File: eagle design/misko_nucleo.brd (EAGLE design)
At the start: 115 x 115 mm, 131 parts, among them CN1 LiPo Battery, IC1 MC1525TT, IC101 ADXL345, IC102 74HCT1G32GW, IC2 TPS63031, IC3 FT230XS, IC4 RN4678_BT_MODULE, IC5 DS1394U-33+, IC6 MAX6818, IC7 SP3012-04UTG, Q1 ABM3B-8MHZ-10-1-U-T, Q2 BSS84, Q3 LFXTAL016178R, SW1 MICROJOYSTICK, SW2 PB6156RSL, SW3 PB6156RSL, U1 SN74LVC1G3157DBVR - BT switch, U2 ATMEGA1281-16AU, U3 TMP36GRTZ, U4 MCP73871-2AAI/ML, U5 SN74LVC1G3157DBVR - GPS switch, X1 FH12-30S-0.5SH

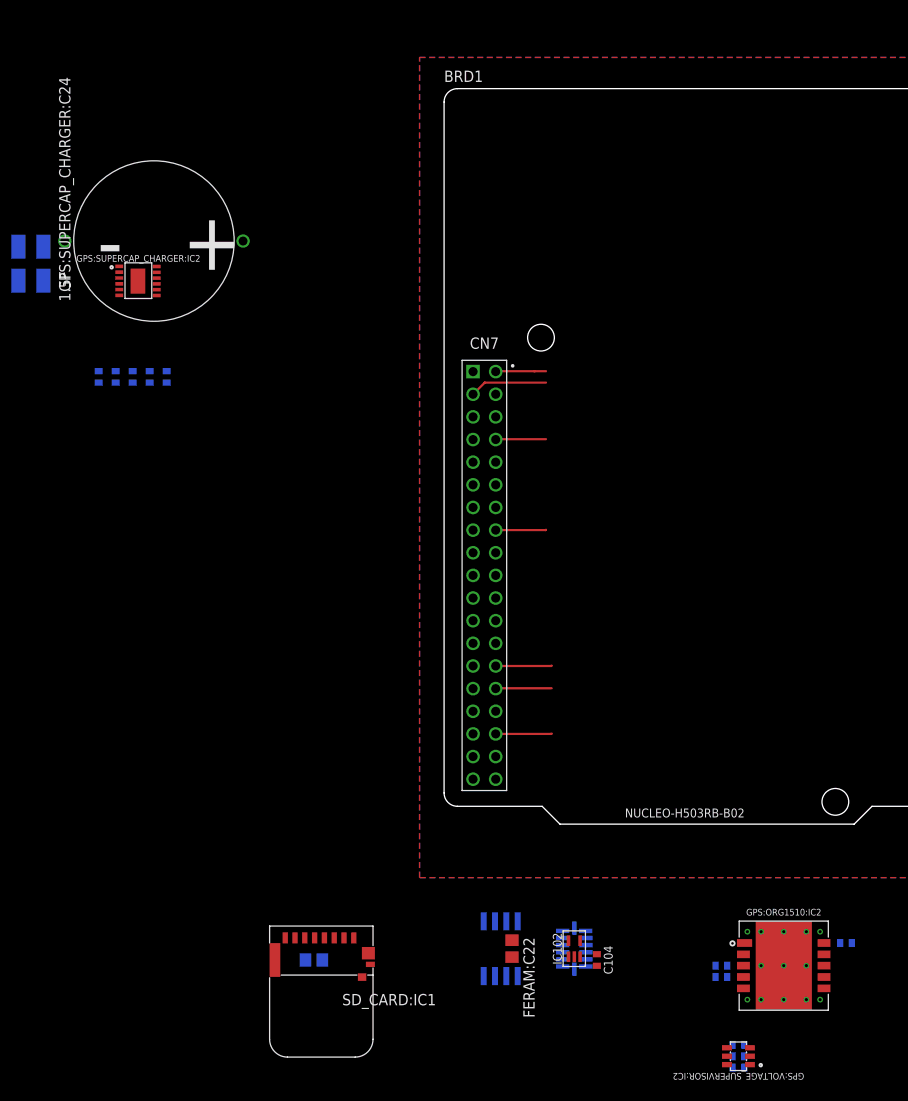
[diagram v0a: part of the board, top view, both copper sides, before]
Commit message: - corrected net names in modules
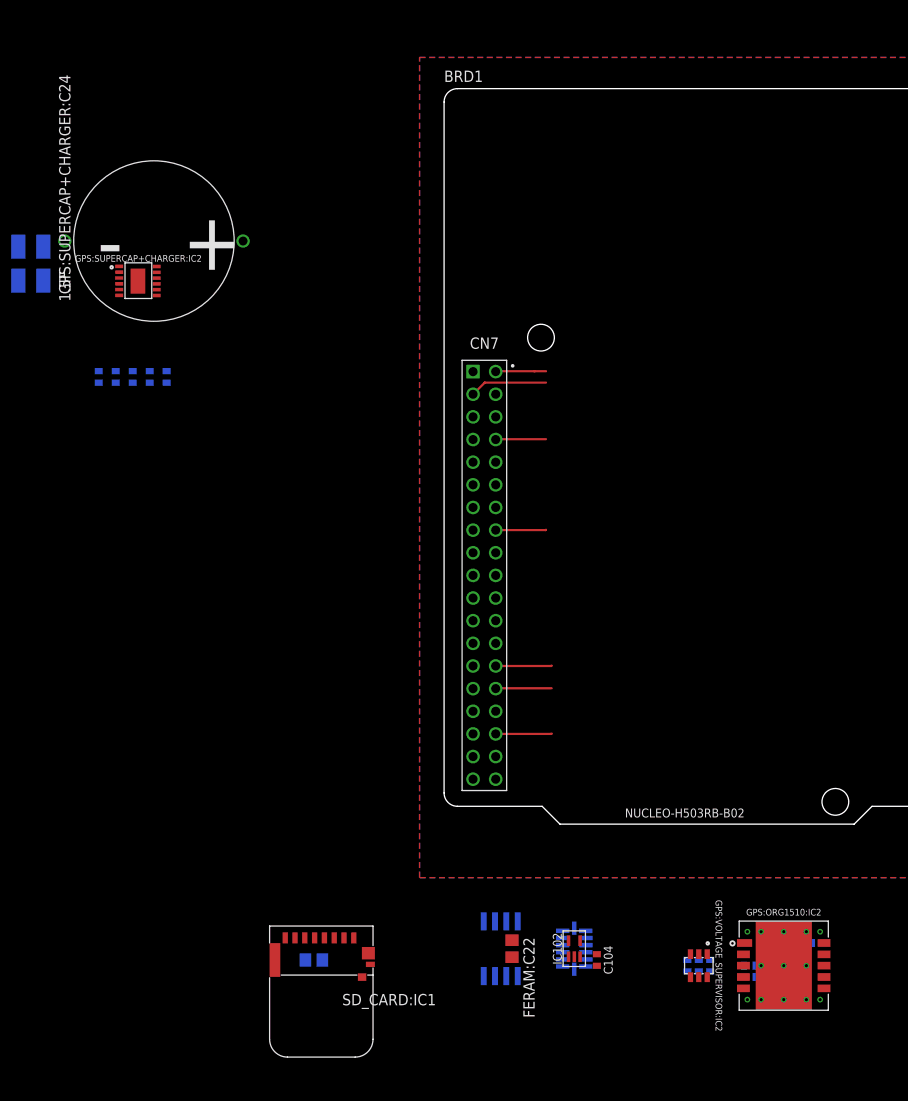
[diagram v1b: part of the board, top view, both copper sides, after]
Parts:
- moved GPS:VOLTAGE_SUPERVISOR:R18 11.9 mm to (29.8, -15.9), turned to 270 degrees
- moved GPS:VOLTAGE_SUPERVISOR:C2 11.1 mm to (28.6, -15.9), turned to 90 degrees
- moved GPS:VOLTAGE_SUPERVISOR:IC2 11.1 mm to (28.6, -15.9), turned to 270 degrees
- moved GPS:VOLTAGE_SUPERVISOR:C1 10.6 mm to (27.3, -15.9), turned to 90 degrees
- moved GPS:ORG1510:C31 3.18 mm to (41.9, -13.3), turned to 0 degrees
- moved GPS:ORG1510:C2 3.18 mm to (34.3, -17.1), turned to 180 degrees
- moved GPS:ORG1510:C22 3.18 mm to (34.3, -15.9), turned to 180 degrees
- renumbered GPS:SUPERCAP_CHARGER:C1 to GPS:SUPERCAP+CHARGER:C1, GPS:SUPERCAP_CHARGER:C24 to GPS:SUPERCAP+CHARGER:C24, GPS:SUPERCAP_CHARGER:C34 to GPS:SUPERCAP+CHARGER:C34, GPS:SUPERCAP_CHARGER:C38 to GPS:SUPERCAP+CHARGER:C38, GPS:SUPERCAP_CHARGER:IC2 to GPS:SUPERCAP+CHARGER:IC2, GPS:SUPERCAP_CHARGER:R14 to GPS:SUPERCAP+CHARGER:R14, GPS:SUPERCAP_CHARGER:R18 to GPS:SUPERCAP+CHARGER:R18, GPS:SUPERCAP_CHARGER:R40 to GPS:SUPERCAP+CHARGER:R40, GPS:SUPERCAP_CHARGER:R41 to GPS:SUPERCAP+CHARGER:R41
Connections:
- net GPS:SUPERCAP_CHARGER:EN renamed GPS:SUPERCAP+CHARGER:EN
- net GPS:SUPERCAP_CHARGER:PFI renamed GPS:SUPERCAP+CHARGER:PFI
- net GPS:SUPERCAP_CHARGER:PFI_RET renamed GPS:SUPERCAP+CHARGER:PFI_RET
- net GPS:SUPERCAP_CHARGER:PROG renamed GPS:SUPERCAP+CHARGER:PROG
- net GPS:SUPERCAP_CHARGER:VMID renamed GPS:SUPERCAP+CHARGER:VMID
- removed net GPS:VOLTAGE_SUPERVISOR:3V3: GPS:VOLTAGE_SUPERVISOR:C2.1, GPS:VOLTAGE_SUPERVISOR:IC2.VDD, GPS:VOLTAGE_SUPERVISOR:R18.2
- new net GPS:VOLTAGE_SUPERVISOR:SENSE: GPS:VOLTAGE_SUPERVISOR:C1.1, GPS:VOLTAGE_SUPERVISOR:IC2.SENSE
- net 3V3: now also GPS:VOLTAGE_SUPERVISOR:C2.1, GPS:VOLTAGE_SUPERVISOR:IC2.VDD, GPS:VOLTAGE_SUPERVISOR:R18.2
- net GPS:VGPS: no longer GPS:VOLTAGE_SUPERVISOR:C1.1, GPS:VOLTAGE_SUPERVISOR:IC2.SENSE

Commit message: - removed not needed components (crystal, voltage reference, etc.) from original schematic
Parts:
- removed C1, C16, C26: 0.1µF, resistor:C0805
- removed C19, C20, C23, C25: 1000µF, rcl:E5-10,5
- removed C2: 10µF, resistor:C0805
- removed C5, C9: 7pF, resistor:C0805
- removed CONN2: JTAG, JTAG 1.27mm 10pin header:TH-JTAG
- removed D1: 1N4148, Diode2:D0805
- removed IC1: MC1525TT, microchip:SOT23
- removed JP1: I2C, jumper:JP4
- removed L2: DL0805-33 33µH, rcl:L0805
- removed Q1: ABM3B-8MHZ-10-1-U-T, ABM3B-8MHZ-10-1-U-T - Quartz Resonator:SMT
- removed R1: 47k, rcl:R0805
- removed R3: 4k7, rcl:R0805
- removed R7, R8: 150k, rcl:R0805
- removed S1: RESET, Wurth_Elektronik_Electromechanic_Switch_rev17c:430152050836
- removed TP1, TP2, TP3: GND, testpad:P1-17Y
- removed TP11: Bluetooth Wakeup Pin, testpad:TP14R
- removed TP4: VCC, testpad:TP14R
- removed TP5: VLiIon Regulated, testpad:TP14R
- removed TP6: VGPS, testpad:TP14R
- removed TP7: Analogue Switch CRTL Pin, testpad:TP14R
- removed TP8: GPS Power CTRL Pin, testpad:B1,27
- removed U3: TMP36GRTZ, TMP36GRTZ:SOT95P280X145-5N
- moved D4 65.5 mm to (157.4, 113.3)
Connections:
- removed net N$31: C1.2, D1.A, R1.1
- net ADXL345_INT1_INTERRUPT_PIN: no longer JP1.3
- net ANALOG_SW_CTRL_PIN: no longer TP7.TP
- net AREF: no longer C2.1, IC1.2
- net AVCC: no longer C26.2, IC1.1, L2.2
- net BLUETOOTH_PROF_IND_PIN: no longer TP11.TP
- net GND: no longer C1.1, C16.2, C19.-, C2.2, C20.-, C23.-, C25.-, C26.1, C5.1, C9.1, CONN2.10_GND, CONN2.2_GND, IC1.3, JP1.1, Q1.GND1, Q1.GND2, R8.2, S1.1, S1.3, TP1.TP, U3.5
- net GPS_POWER_CTL_PIN: no longer TP8.TP
- net JTAG_TCL_PIN: no longer CONN2.1_JTAG_TCK
- net JTAG_TDI_PIN: no longer CONN2.9_JTAG_TDI
- net JTAG_TDO_PIN: no longer CONN2.3_JTAG_TDO
- net JTAG_TMS_PIN: no longer CONN2.5_JTAG_TMS
- net N$6: no longer C19.+, C20.+, C23.+, C25.+
- net RESET: no longer CONN2.6_JTAG_RST, R1.2, R3.2, S1.2, S1.4
- net RTC_INT_INTERRUPT_PIN: no longer JP1.4
- net TMP36_VSENSE_PIN: no longer U3.1
- net VCC: no longer C16.1, CONN2.4_VCC, D1.C, JP1.2, L2.1, R3.1, R7.1, TP3.TP, TP4.TP, U3.2, U3.4
- net VCC_SENSE_PIN: no longer R7.2, R8.1
- net VGPS: no longer TP6.TP
- net VUSB: no longer TP2.TP
- net V_LIION_REGULATED: no longer TP5.TP
- net XTAL1: no longer C9.2, Q1.Q2
- net XTAL2: no longer C5.2, Q1.Q1
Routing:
- net VCC: track 385.2 -> 275.0 mm, vias 15 -> 14
- net N$6: track 106.0 -> 0.00 mm
- net RESET: track 64.8 -> 0.00 mm, vias 3 -> 0
- net VGPS: track 52.4 -> 9.08 mm, vias 1 -> 0
- net GND: track 47.2 -> 25.2 mm, vias 37 -> 3
- net VCC_SENSE_PIN: track 14.1 -> 0.00 mm, vias 1 -> 0
- net TMP36_VSENSE_PIN: track 14.1 -> 0.00 mm, vias 3 -> 0
- net AVCC: track 12.1 -> 0.00 mm, vias 1 -> 0
- net JTAG_TDO_PIN: track 11.8 -> 0.00 mm, vias 2 -> 0
- net OLD_5V0: track 57.7 -> 46.4 mm, vias 6 -> 5
- net AREF: track 11.0 -> 0.00 mm, vias 1 -> 0
- net JTAG_TCL_PIN: track 10.1 -> 0.00 mm
- net V_LIION_REGULATED: track 41.0 -> 30.9 mm
- net JTAG_TDI_PIN: track 9.86 -> 0.00 mm
- net JTAG_TMS_PIN: track 9.47 -> 0.00 mm
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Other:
- board size 115 x 115 mm -> 115 x 73 mm
- board text removed: "BT PROF IND"
- board text removed: "GPS PWR CTRL"
- board text removed: "I2C"
- board text removed: "JTAG"
- board text removed: "RESET"

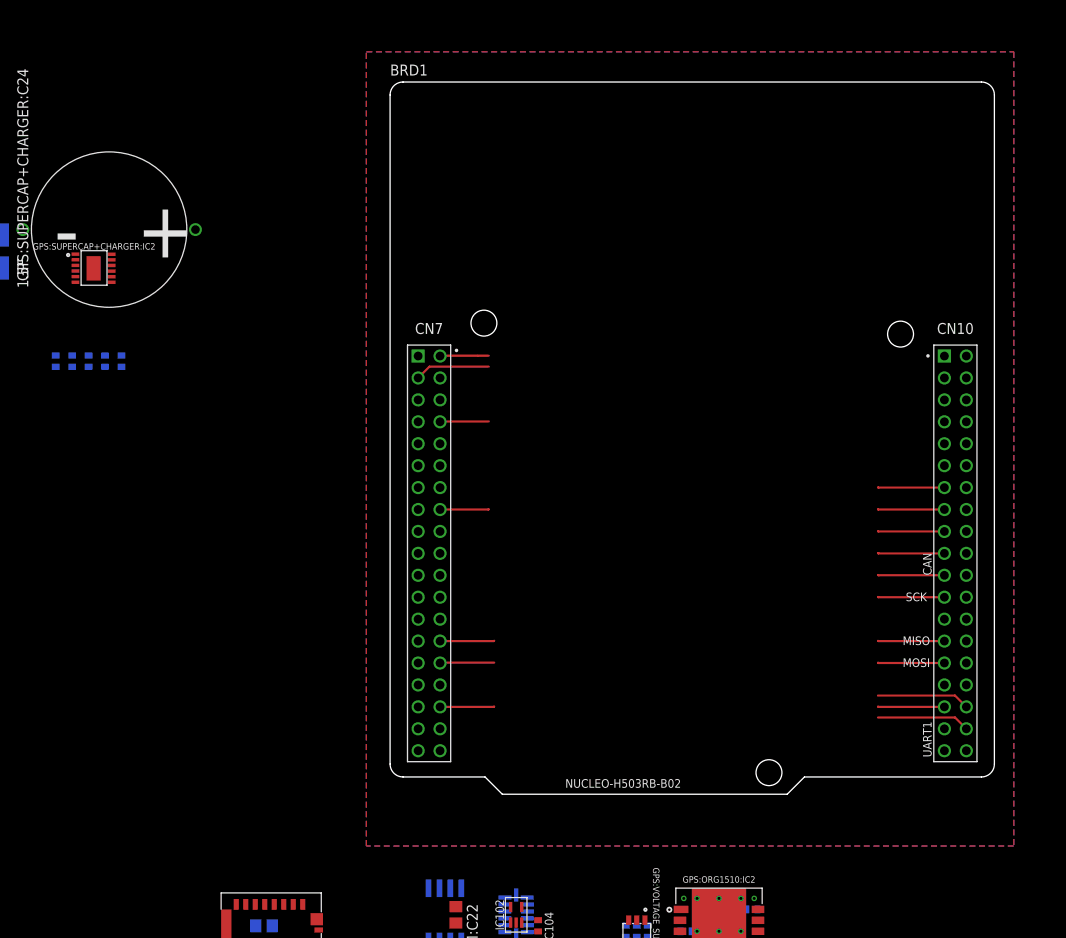
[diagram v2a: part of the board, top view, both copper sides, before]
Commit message: - added/coded and routed ORG1510-MK4 GPS module reset and LTC4425 SuperCap Charger enable pins
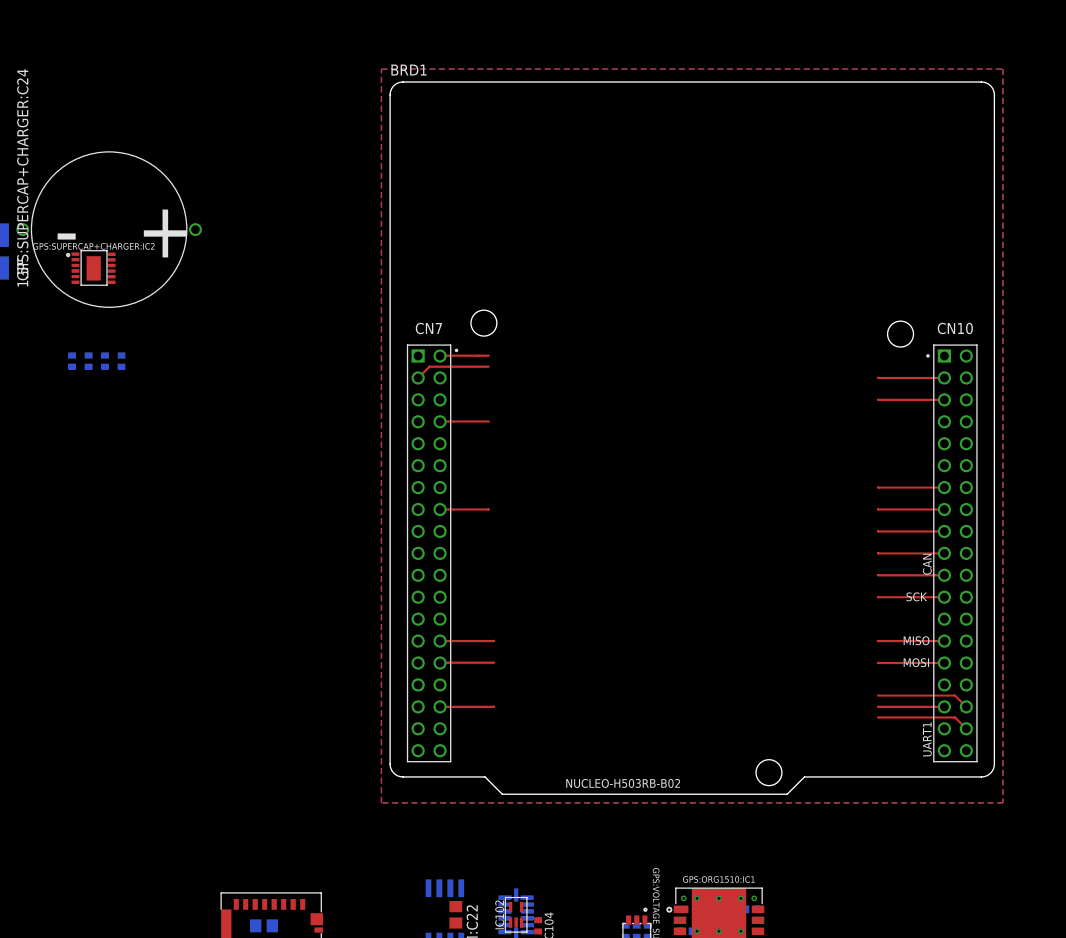
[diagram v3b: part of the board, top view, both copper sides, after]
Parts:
- removed GPS:ORG1510:IC2: ORG1510MK4, ORG1510-MK4 GPS module:PACKAGE
- removed GPS:SUPERCAP+CHARGER:R18: 1k, resistor:R0402
- added GPS:ORG1510:IC1: ORG1510-MK4, ORG1510-MK4 GPS module:SMD
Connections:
- removed net GPS:SUPERCAP+CHARGER:EN: GPS:SUPERCAP+CHARGER:IC2.EN, GPS:SUPERCAP+CHARGER:R18.2
- removed net PB6: BRD1.CN10_3
- removed net PB7: BRD1.CN10_5
- new net GPS_!RESET!: BRD1.CN10_3, GPS:ORG1510:IC1.!RESET!_8
- new net SUPERCAP_!EN!: BRD1.CN10_5, GPS:SUPERCAP+CHARGER:IC2.EN
- net 3V3: no longer GPS:SUPERCAP+CHARGER:R18.1
- net GND: now also GPS:ORG1510:IC1.5_GND, GPS:ORG1510:IC1.GND1, GPS:ORG1510:IC1.GND10, GPS:ORG1510:IC1.GND11, GPS:ORG1510:IC1.GND12, GPS:ORG1510:IC1.GND13, GPS:ORG1510:IC1.GND14, GPS:ORG1510:IC1.GND15, GPS:ORG1510:IC1.GND2, GPS:ORG1510:IC1.GND4, GPS:ORG1510:IC1.GND5, GPS:ORG1510:IC1.GND6, GPS:ORG1510:IC1.GND7, GPS:ORG1510:IC1.GND8, GPS:ORG1510:IC1.GND9; no longer GPS:ORG1510:IC2.5_GND, GPS:ORG1510:IC2.GND1, GPS:ORG1510:IC2.GND10, GPS:ORG1510:IC2.GND11, GPS:ORG1510:IC2.GND12, GPS:ORG1510:IC2.GND13, GPS:ORG1510:IC2.GND14, GPS:ORG1510:IC2.GND15, GPS:ORG1510:IC2.GND2, GPS:ORG1510:IC2.GND4, GPS:ORG1510:IC2.GND5, GPS:ORG1510:IC2.GND6, GPS:ORG1510:IC2.GND7, GPS:ORG1510:IC2.GND8, GPS:ORG1510:IC2.GND9
- net GPS:GPS_ON_OFF: now also GPS:ORG1510:IC1.1_ON_OFF; no longer GPS:ORG1510:IC2.1_ON_OFF
- net GPS:VGPS: now also GPS:ORG1510:IC1.4_VCC; no longer GPS:ORG1510:IC2.4_VCC
- net GPS_SW_SERIAL_TX: now also GPS:ORG1510:IC1.RX_10; no longer GPS:ORG1510:IC2.RX_10
- net GPS_TX: now also GPS:ORG1510:IC1.3_TX; no longer GPS:ORG1510:IC2.3_TX
- net GPS_WKUP: now also GPS:ORG1510:IC1.WAKEUP_6; no longer GPS:ORG1510:IC2.WAKEUP_6
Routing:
- net SUPERCAP_!EN!: track 0.00 -> 7.71 mm
- net GPS_!RESET!: track 0.00 -> 7.71 mm

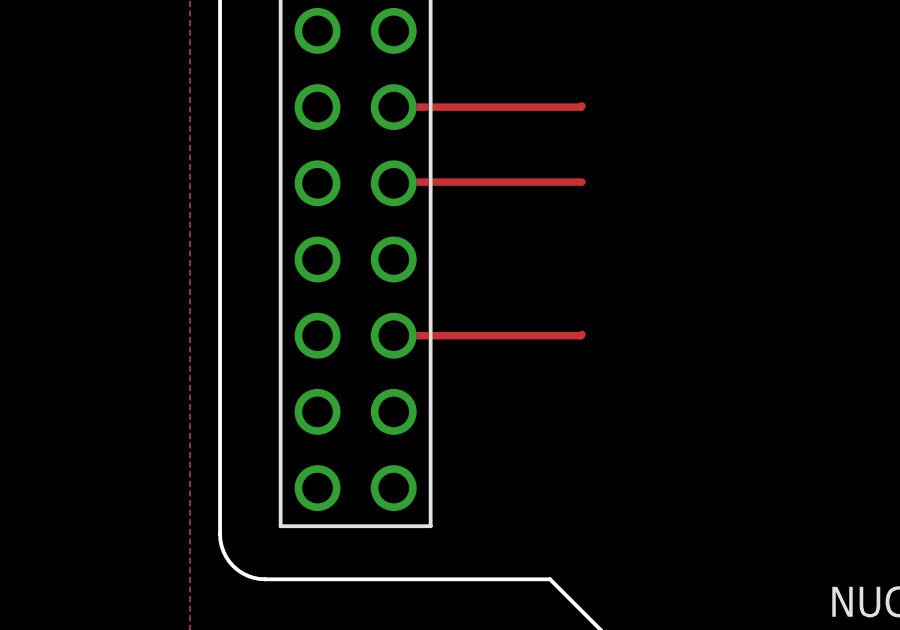
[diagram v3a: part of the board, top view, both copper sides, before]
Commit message: - added MPU config for read-only register readout - configured ADC to work on timer1 CC trigger - implemented Vgps, Vbat, Vrefint and Temperature ADC measurement over a 1s average
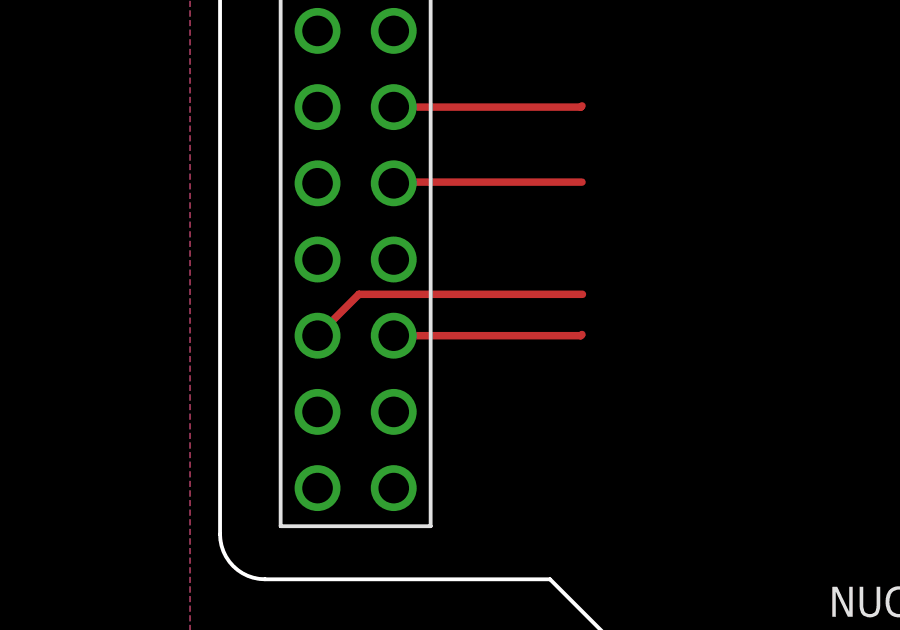
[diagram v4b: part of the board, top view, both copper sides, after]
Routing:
- net VBAT: track 0.00 -> 9.40 mm
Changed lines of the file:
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@@
 <setting verticaltext="up"/>
 </settings>
-<grid distance="1" unitdist="mm" unit="mm" style="lines" multiple="1" display="yes" altdistance="0.005" altunitdist="mm" altunit="mm"/>
+<grid distance="0.25" unitdist="mm" unit="mm" style="lines" multiple="1" display="yes" altdistance="0.005" altunitdist="mm" altunit="mm"/>
 <layers>
 <layer number="1" name="Top" color="4" fill="1" visible="yes" active="yes"/>
@@
 <signal name="VBAT" class="2">
 <contactref element="BRD1" pad="CN7_33"/>
+<wire x1="4.63" y1="11.5" x2="12.08" y2="11.5" width="0.25" layer="1"/>
+<wire x1="3.25" y1="10.12" x2="4.63" y2="11.5" width="0.25" layer="1"/>
 </signal>
 <signal name="VDD">
